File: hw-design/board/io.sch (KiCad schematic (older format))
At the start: 16 parts, among them P4 FOOT, P5 10K POT, SW2 SP3T

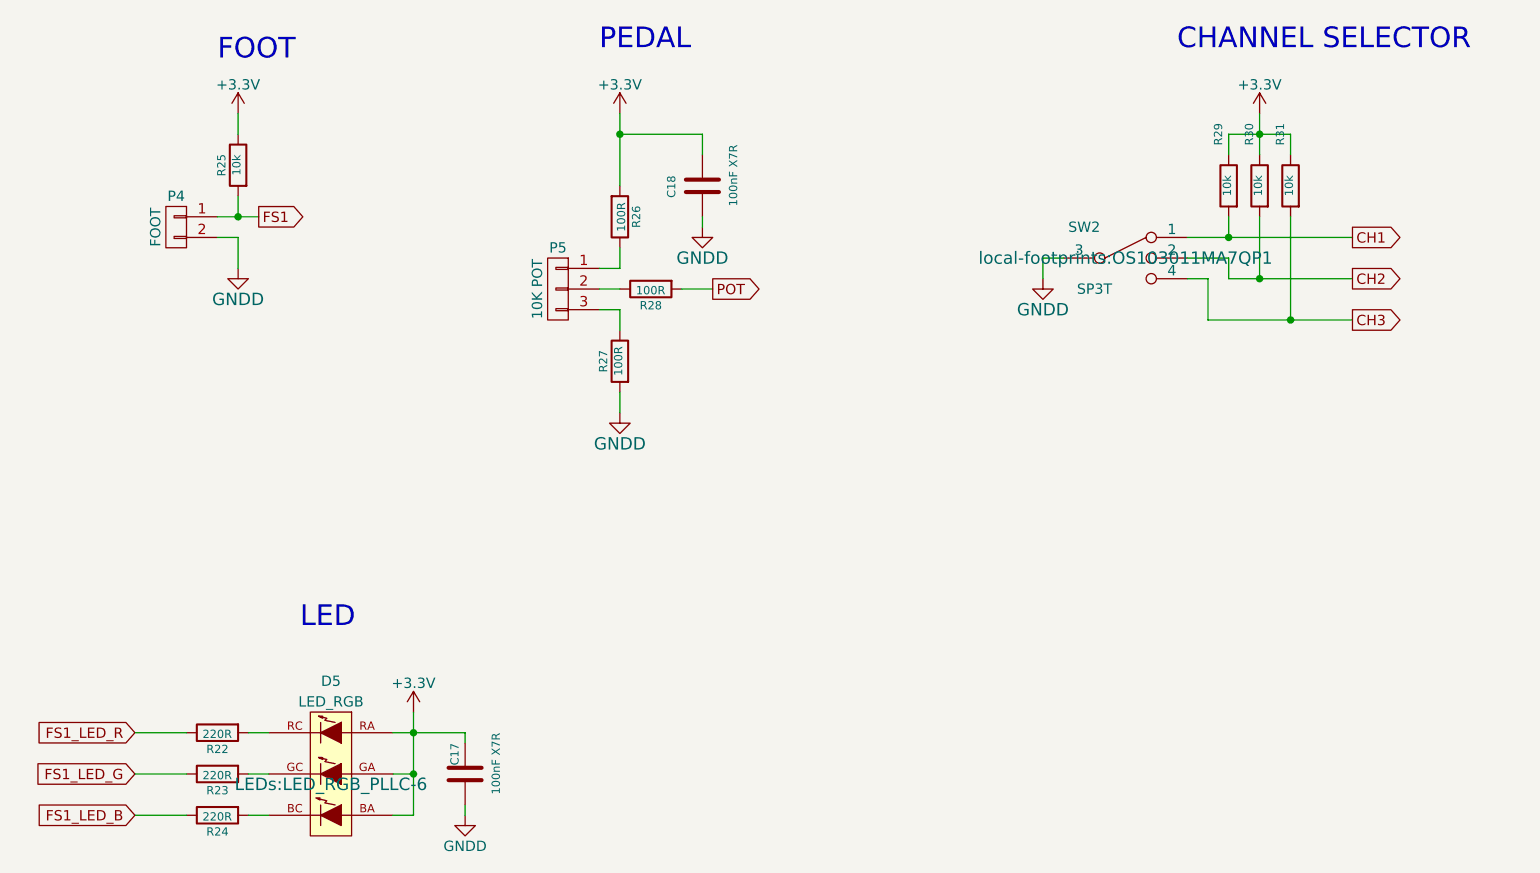
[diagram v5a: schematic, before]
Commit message: sch: fixing VBUS signal and FS1 I/O
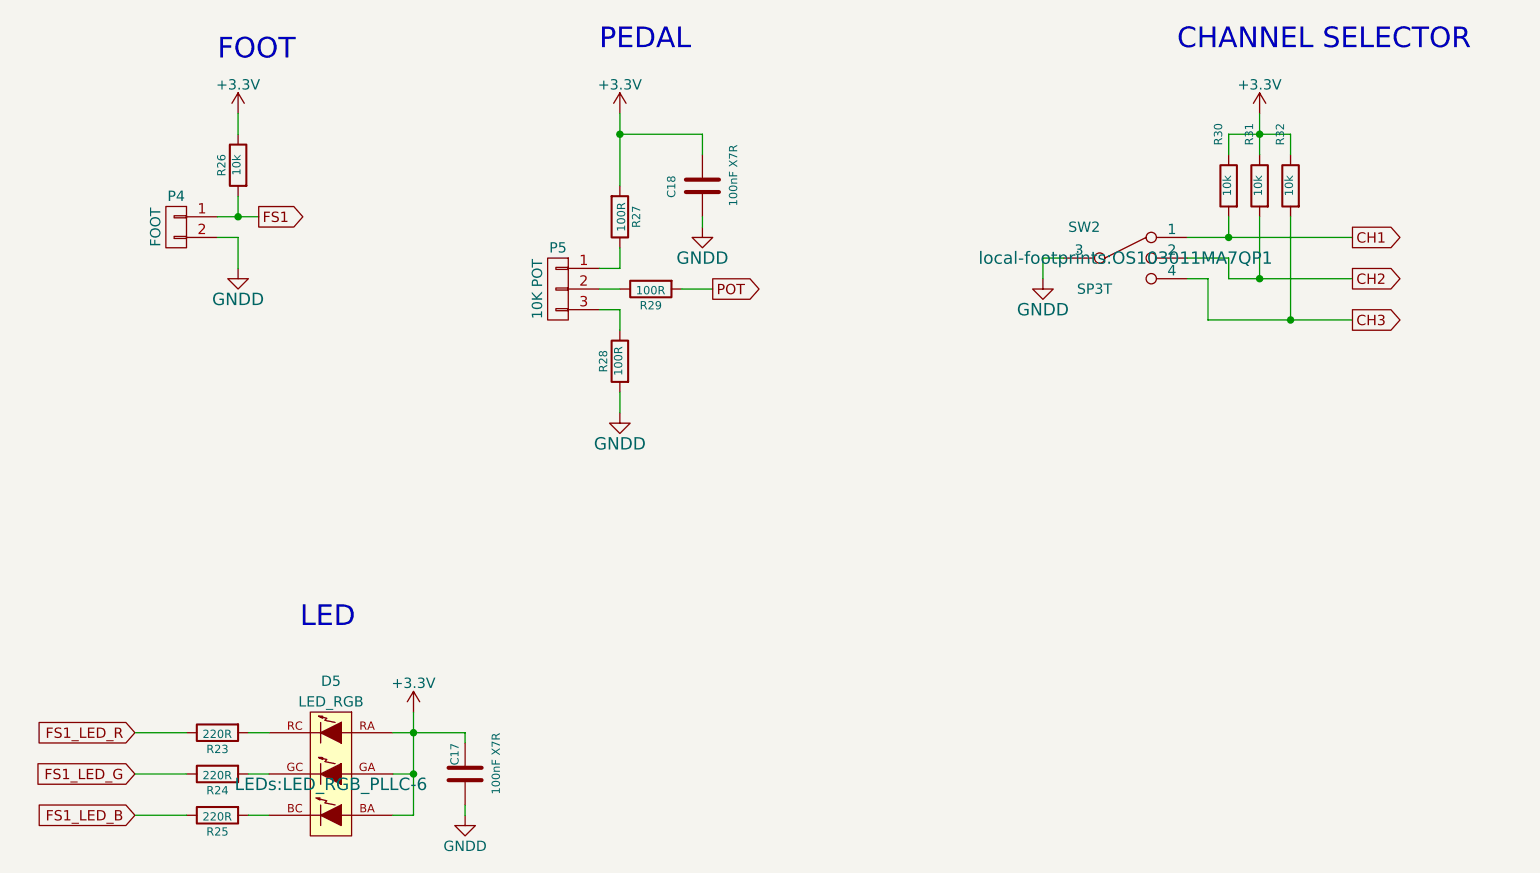
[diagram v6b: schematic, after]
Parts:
- renumbered R22 to R23, R23 to R24, R24 to R25, R25 to R26, R26 to R27, R27 to R28, R28 to R29, R29 to R30, R30 to R31, R31 to R32
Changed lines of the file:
@@
 $EndDescr
 $Comp
-L R R29
+L R R30
 U 1 1 54CBEC23
 P 6850 1750
-F 0 "R29" V 6900 2000 40  0000 C CNN
+F 0 "R30" V 6900 2000 40  0000 C CNN
 F 1 "10k" V 6857 1751 40  0000 C CNN
 F 2 "Resistors_SMD:R_0603" V 6780 1750 30  0001 C CNN
@@
 $EndComp
 $Comp
-L R R30
+L R R31
 U 1 1 54CBEC30
 P 7000 1750
-F 0 "R30" V 7050 2000 40  0000 C CNN
+F 0 "R31" V 7050 2000 40  0000 C CNN
 F 1 "10k" V 7007 1751 40  0000 C CNN
 F 2 "Resistors_SMD:R_0603" V 6930 1750 30  0001 C CNN
@@
 $EndComp
 $Comp
-L R R31
+L R R32
 U 1 1 54CBEC37
 P 7150 1750
-F 0 "R31" V 7200 2000 40  0000 C CNN
+F 0 "R32" V 7200 2000 40  0000 C CNN
 F 1 "10k" V 7157 1751 40  0000 C CNN
 F 2 "Resistors_SMD:R_0603" V 7080 1750 30  0001 C CNN
@@
 $EndComp
 $Comp
-L R R25
+L R R26
 U 1 1 54CBEC53
 P 2050 1650
-F 0 "R25" V 2130 1650 40  0000 C CNN
+F 0 "R26" V 2130 1650 40  0000 C CNN
 F 1 "10k" V 2057 1651 40  0000 C CNN
 F 2 "Resistors_SMD:R_0603" V 1980 1650 30  0001 C CNN
@@
 $EndComp
 $Comp
-L R R26
+L R R27
 U 1 1 54CBEC6F
 P 3900 1900
-F 0 "R26" V 3980 1900 40  0000 C CNN
+F 0 "R27" V 3980 1900 40  0000 C CNN
 F 1 "100R" V 3907 1901 40  0000 C CNN
 F 2 "Resistors_SMD:R_0603" V 3830 1900 30  0001 C CNN
@@
 $EndComp
 $Comp
-L R R27
+L R R28
 U 1 1 54CBEC82
 P 3900 2600
-F 0 "R27" V 3980 2600 40  0000 C CNN
+F 0 "R28" V 3980 2600 40  0000 C CNN
 F 1 "100R" V 3907 2601 40  0000 C CNN
 F 2 "Resistors_SMD:R_0603" V 3830 2600 30  0001 C CNN
@@
 $EndComp
 $Comp
-L R R28
+L R R29
 U 1 1 54CBEC89
 P 4050 2250
-F 0 "R28" V 4130 2250 40  0000 C CNN
+F 0 "R29" V 4130 2250 40  0000 C CNN
 F 1 "100R" V 4057 2251 40  0000 C CNN
 F 2 "Resistors_SMD:R_0603" V 3980 2250 30  0001 C CNN
@@
 $EndComp
 $Comp
-L GNDD #PWR060
+L GNDD #PWR061
 U 1 1 54E65047
 P 2050 2150
-F 0 "#PWR060" H 2050 1900 60  0001 C CNN
+F 0 "#PWR061" H 2050 1900 60  0001 C CNN
 F 1 "GNDD" H 2050 2000 60  0000 C CNN
 F 2 "" H 2050 2150 60  0000 C CNN
@@
 $EndComp
 $Comp
-L GNDD #PWR061
+L GNDD #PWR062
 U 1 1 54E661EA
 P 3900 2850
-F 0 "#PWR061" H 3900 2600 60  0001 C CNN
+F 0 "#PWR062" H 3900 2600 60  0001 C CNN
 F 1 "GNDD" H 3900 2700 60  0000 C CNN
 F 2 "" H 3900 2850 60  0000 C CNN
@@
 $EndComp
 $Comp
-L GNDD #PWR062
+L GNDD #PWR063
 U 1 1 54E66D8A
 P 4300 1950
-F 0 "#PWR062" H 4300 1700 60  0001 C CNN
+F 0 "#PWR063" H 4300 1700 60  0001 C CNN
 F 1 "GNDD" H 4300 1800 60  0000 C CNN
 F 2 "" H 4300 1950 60  0000 C CNN
@@
 $EndComp
 $Comp
-L GNDD #PWR063
+L GNDD #PWR064
 U 1 1 54E753B2
 P 5950 2200
-F 0 "#PWR063" H 5950 1950 60  0001 C CNN
+F 0 "#PWR064" H 5950 1950 60  0001 C CNN
 F 1 "GNDD" H 5950 2050 60  0000 C CNN
 F 2 "" H 5950 2200 60  0000 C CNN
@@
 $EndComp
 $Comp
-L +3.3V #PWR064
+L +3.3V #PWR065
 U 1 1 556F3C3C
 P 2050 1400
-F 0 "#PWR064" H 2050 1250 50  0001 C CNN
+F 0 "#PWR065" H 2050 1250 50  0001 C CNN
 F 1 "+3.3V" H 2050 1540 50  0000 C CNN
 F 2 "" H 2050 1400 60  0000 C CNN
@@
 $EndComp
 $Comp
-L +3.3V #PWR065
+L +3.3V #PWR066
 U 1 1 556F3CC5
 P 3900 1400
-F 0 "#PWR065" H 3900 1250 50  0001 C CNN
+F 0 "#PWR066" H 3900 1250 50  0001 C CNN
 F 1 "+3.3V" H 3900 1540 50  0000 C CNN
 F 2 "" H 3900 1400 60  0000 C CNN
@@
 $EndComp
 $Comp
-L +3.3V #PWR066
+L +3.3V #PWR067
 U 1 1 556F428C
 P 7000 1400
-F 0 "#PWR066" H 7000 1250 50  0001 C CNN
+F 0 "#PWR067" H 7000 1250 50  0001 C CNN
 F 1 "+3.3V" H 7000 1540 50  0000 C CNN
 F 2 "" H 7000 1400 60  0000 C CNN
@@
 $EndComp
 $Comp
-L +3.3V #PWR067
+L +3.3V #PWR068
 U 1 1 557A9EA8
 P 2900 4300
-F 0 "#PWR067" H 2900 4150 50  0001 C CNN
+F 0 "#PWR068" H 2900 4150 50  0001 C CNN
 F 1 "+3.3V" H 2900 4440 50  0000 C CNN
 F 2 "" H 2900 4300 60  0000 C CNN
@@
 $EndComp
 $Comp
-L GNDD #PWR068
+L GNDD #PWR069
 U 1 1 557AA05D
 P 3150 4800
-F 0 "#PWR068" H 3150 4550 50  0001 C CNN
+F 0 "#PWR069" H 3150 4550 50  0001 C CNN
 F 1 "GNDD" H 3150 4650 50  0000 C CNN
 F 2 "" H 3150 4800 60  0000 C CNN
@@
 $EndComp
 $Comp
-L R R22
+L R R23
 U 1 1 557AA39A
 P 1950 4400
-F 0 "R22" V 2030 4400 40  0000 C CNN
+F 0 "R23" V 2030 4400 40  0000 C CNN
 F 1 "220R" V 1957 4401 40  0000 C CNN
 F 2 "Resistors_SMD:R_0603" V 1880 4400 30  0001 C CNN
@@
 $EndComp
 $Comp
-L R R23
+L R R24
 U 1 1 557AADB8
 P 1950 4600
-F 0 "R23" V 2030 4600 40  0000 C CNN
+F 0 "R24" V 2030 4600 40  0000 C CNN
 F 1 "220R" V 1957 4601 40  0000 C CNN
 F 2 "Resistors_SMD:R_0603" V 1880 4600 30  0001 C CNN
@@
 $EndComp
 $Comp
-L R R24
+L R R25
 U 1 1 557AAE1B
 P 1950 4800
-F 0 "R24" V 2030 4800 40  0000 C CNN
+F 0 "R25" V 2030 4800 40  0000 C CNN
 F 1 "220R" V 1957 4801 40  0000 C CNN
 F 2 "Resistors_SMD:R_0603" V 1880 4800 30  0001 C CNN
